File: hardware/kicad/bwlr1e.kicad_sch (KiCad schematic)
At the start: 66 parts, among them Q1 AO3407, Q2 DMG1012UW, SW3 RESET, SW4 BOOT, U1 BME680, U2 RAK3172, U3 AEM10941-QFN, U4 XC6215

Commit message: revision 2
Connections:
- net GND: now also SC1.2 (-), SC3.2 (-)
- net SOLAR+: now also SC2.1 (+), SC4.1 (+)
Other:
- note removed: "TODO: Change to Parallel"
- moved on the sheet: BT1, C1, C2, C4, C6, C7, C8, JP3, JP4, L2, L3, Q1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

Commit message: revision 3
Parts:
- added TP12: PRIMIN, TestPoint:TestPoint_Pad_D2.0mm, symbol Connector:TestPoint
- added TP13: GND, TestPoint:TestPoint_Pad_D2.0mm, symbol Connector:TestPoint
- TP1: value 3V3 -> PRIMIN
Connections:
- net GND: now also TP13.1
- net EXT_3V3 renamed PRIMIN
- net PRIMIN: now also TP12.1
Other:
- note added: "Options: 1. R10 = 1M, R11 = 100K, R14 = 400K, R15 = 1M, JP5 = PRIMIN 2. R10, R11, R14, and R15 = 0, R16, JP5 = Open 3. R10 = 1M, R11 = 100K, R14 = 400K, R15 = 1M, JP5 = BUCK"
- note added: "Primary Battery"
- note removed: "Experimental Options: 1. R10 = 1M, R11 = 100K, R14 = 400K, R15 = 1M, JP5 = EXT_3V3 2. R10, R11, R14, and R15 = 0, R16, JP5 = Open 3. R10 = 1M, R11 = 100K, R14 = 400K, R15 = 1M, JP5 = BUCK"
- note removed: "External Charging"
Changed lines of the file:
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@@
   (title_block
     (title "Teapot BWLR1E")
-    (date "2022-08-03")
-    (rev "2")
+    (date "2022-08-21")
+    (rev "3")
     (company "Teapot Laboratories")
   )
@@
     (stroke (width 0) (type default) (color 0 0 0 0))
   )
+  (wire (pts (xy 396.875 69.85) (xy 408.305 69.85))
+    (stroke (width 0) (type default) (color 0 0 0 0))
+  )
   (wire (pts (xy 138.43 121.92) (xy 138.43 127))
     (stroke (width 0) (type default) (color 0 0 0 0))
@@
     (stroke (width 0) (type default) (color 0 0 0 0))
   )
+  (wire (pts (xy 396.875 74.295) (xy 404.495 74.295))
+    (stroke (width 0) (type default) (color 0 0 0 0))
+  )
   (wire (pts (xy 86.36 165.1) (xy 86.36 166.37))
     (stroke (width 0) (type default) (color 0 0 0 0))
@@
     (effects (font (size 1.27 1.27)) (justify left bottom))
   )
-  (text "External Charging" (at 394.97 86.36 0)
+  (text "Primary Battery" (at 396.875 86.36 0)
     (effects (font (size 1.27 1.27)) (justify left bottom))
   )
@@
     (effects (font (size 1.27 1.27)) (justify left bottom))
   )
-  (text "Experimental Options:\n1. R10 = 1M, R11 = 100K, R14 = 400K, R15 = 1M, JP5 = EXT_3V3\n2. R10, R11, R14, and R15 = 0, R16, JP5 = Open\n3. R10 = 1M, R11 = 100K, R14 = 400K, R15 = 1M, JP5 = BUCK"
+  (text "Options:\n1. R10 = 1M, R11 = 100K, R14 = 400K, R15 = 1M, JP5 = PRIMIN\n2. R10, R11, R14, and R15 = 0, R16, JP5 = Open\n3. R10 = 1M, R11 = 100K, R14 = 400K, R15 = 1M, JP5 = BUCK"
     (at 343.535 19.685 0)
     (effects (font (size 1 1)) (justify left bottom))
@@
     (effects (font (size 1.27 1.27)) (justify left bottom))
   )
-  (label "EXT_3V3" (at 297.18 103.505 180)
+  (label "PRIMIN" (at 297.18 103.505 180)
     (effects (font (size 1.27 1.27)) (justify right bottom))
   )
@@
     (effects (font (size 1.27 1.27)) (justify right bottom))
   )
-  (label "EXT_3V3" (at 382.905 59.055 180)
+  (label "PRIMIN" (at 382.905 59.055 180)
     (effects (font (size 1.27 1.27)) (justify right bottom))
   )
@@
     (effects (font (size 1.27 1.27)) (justify left bottom))
   )
-  (label "EXT_3V3" (at 407.035 46.355 180)
+  (label "PRIMIN" (at 407.035 46.355 180)
     (effects (font (size 1.27 1.27)) (justify right bottom))
   )
@@
     (effects (font (size 1.27 1.27)) (justify right bottom))
   )
+  (label "PRIMIN" (at 408.305 69.85 180)
+    (effects (font (size 1.27 1.27)) (justify right bottom))
+  )
   (label "USER1" (at 223.52 166.37 180)
     (effects (font (size 1.27 1.27)) (justify right bottom))
@@
     (pin "2")
   )
+  (symbol (lib_id "power:GND") (at 404.495 74.295 0) (unit 1)
+    (in_bom yes) (on_board yes) (fields_autoplaced)
+    (property "Reference" "#PWR0135" (id 0) (at 404.495 80.645 0)
+      (effects (font (size 1.27 1.27)) hide)
+    )
+    (property "Value" "GND" (id 1) (at 404.495 79.375 0))
+    (property "Footprint" "" (id 2) (at 404.495 74.295 0)
+      (effects (font (size 1.27 1.27)) hide)
+    )
+    (property "Datasheet" "" (id 3) (at 404.495 74.295 0)
+      (effects (font (size 1.27 1.27)) hide)
+    )
+    (pin "1")
+  )
   (symbol (lib_id "Device:LED") (at 281.305 170.815 180) (unit 1)
     (in_bom yes) (on_board yes)
@@
     (in_bom yes) (on_board yes)
     (property "Reference" "TP1" (id 0) (at 271.78 103.505 90))
-    (property "Value" "3V3" (id 1) (at 278.13 103.505 90))
+    (property "Value" "PRIMIN" (id 1) (at 278.13 103.505 90))
     (property "Footprint" "TestPoint:TestPoint_Pad_1.5x1.5mm" (id 2) (at 285.75 98.425 0)
       (effects (font (size 1.27 1.27)) hide)
@@
     (pin "1")
   )
+  (symbol (lib_id "Connector:TestPoint") (at 396.875 74.295 90) (unit 1)
+    (in_bom yes) (on_board yes)
+    (property "Reference" "TP13" (id 0) (at 382.905 74.295 90))
+    (property "Value" "GND" (id 1) (at 389.255 74.295 90))
+    (property "Footprint" "TestPoint:TestPoint_Pad_D2.0mm" (id 2) (at 396.875 69.215 0)
+      (effects (font (size 1.27 1.27)) hide)
+    )
+    (property "Datasheet" "~" (id 3) (at 396.875 69.215 0)
+      (effects (font (size 1.27 1.27)) hide)
+    )
+    (pin "1")
+  )
   (symbol (lib_id "power:GND") (at 194.945 121.92 0) (unit 1)
     (in_bom yes) (on_board yes)
@@
     (pin "3")
   )
+  (symbol (lib_id "Connector:TestPoint") (at 396.875 69.85 90) (unit 1)
+    (in_bom yes) (on_board yes)
+    (property "Reference" "TP12" (id 0) (at 382.905 69.85 90))
+    (property "Value" "PRIMIN" (id 1) (at 389.255 69.85 90))
+    (property "Footprint" "TestPoint:TestPoint_Pad_D2.0mm" (id 2) (at 396.875 64.77 0)
+      (effects (font (size 1.27 1.27)) hide)
+    )
+    (property "Datasheet" "~" (id 3) (at 396.875 64.77 0)
+      (effects (font (size 1.27 1.27)) hide)
+    )
+    (pin "1")
+  )
   (symbol (lib_id "power:GND") (at 48.26 134.62 0) (unit 1)
     (in_bom yes) (on_board yes) (fields_autoplaced)
@@
       (reference "#PWR0134") (unit 1) (value "+3V3") (footprint "")
     )
+    (path "/1e90f9d8-c727-4558-8e6d-fc3c11796233"
+      (reference "#PWR0135") (unit 1) (value "GND") (footprint "")
+    )
     (path "/c9f4c90b-d12e-49a7-861d-d88f5120271b"
       (reference "BT1") (unit 1) (value "3.7v LiPo") (footprint "Connector_JST:JST_PH_S2B-PH-K_1x02_P2.00mm_Horizontal")
@@
     )
     (path "/2a1338b5-8d40-458a-9d24-bac76b51b578"
-      (reference "TP1") (unit 1) (value "3V3") (footprint "TestPoint:TestPoint_Pad_1.5x1.5mm")
+      (reference "TP1") (unit 1) (value "PRIMIN") (footprint "TestPoint:TestPoint_Pad_1.5x1.5mm")
     )
     (path "/b524f92a-354c-4e70-b2ab-52ea6b8a451a"
@@
       (reference "TP11") (unit 1) (value "SOLAR-") (footprint "TestPoint:TestPoint_Pad_D1.5mm")
     )
+    (path "/81b383ec-6014-4264-9dd9-3b100f125f97"
+      (reference "TP12") (unit 1) (value "PRIMIN") (footprint "TestPoint:TestPoint_Pad_D2.0mm")
+    )
+    (path "/5e32705b-900d-4567-9e7f-6cf99fe286b8"
+      (reference "TP13") (unit 1) (value "GND") (footprint "TestPoint:TestPoint_Pad_D2.0mm")
+    )
     (path "/33f66e46-4d60-4c90-84ca-37ca92e2ffdc"

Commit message: move battery measurement to PB3
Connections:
- net BATT_MEAS: now also U2.32 (PB3/ADC1); no longer U2.3 (PA15/ADC5)
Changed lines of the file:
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@@
   (no_connect (at 67.31 154.94))
   (no_connect (at 67.31 134.62))
-  (no_connect (at 67.31 132.08))
+  (no_connect (at 67.31 142.24))
   (no_connect (at 118.11 137.16))
   (no_connect (at 118.11 139.7))
@@
     (stroke (width 0) (type default) (color 0 0 0 0))
   )
-  (wire (pts (xy 55.88 142.24) (xy 67.31 142.24))
+  (wire (pts (xy 55.88 132.08) (xy 67.31 132.08))
     (stroke (width 0) (type default) (color 0 0 0 0))
   )
@@
     (effects (font (size 1.27 1.27)) (justify right bottom))
   )
-  (label "BATT_MEAS" (at 55.88 142.24 0)
-    (effects (font (size 1.27 1.27)) (justify left bottom))
-  )
+  (label "BATT_MEAS" (at 55.88 132.08 0)
+    (effects (font (size 1.27 1.27)) (justify left bottom))
+  )

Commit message: change jst type to smt
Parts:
- BT1: value 3.7v LiPo -> (none); footprint Connector_JST:JST_PH_S2B-PH-K_1x02_P2.00mm_Horizontal -> (none)
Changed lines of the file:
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@@
   (title_block
     (title "Teapot BWLR1E")
-    (date "2022-08-21")
-    (rev "3")
+    (date "2022-10-22")
+    (rev "4")
     (company "Teapot Laboratories")
   )
@@
       (effects (font (size 1.27 1.27)) (justify left))
     )
-    (property "Value" "3.7v LiPo" (id 1) (at 36.195 70.9929 0)
+    (property "Value" "" (id 1) (at 36.195 70.9929 0)
       (effects (font (size 1.27 1.27)) (justify left))
     )
-    (property "Footprint" "Connector_JST:JST_PH_S2B-PH-K_1x02_P2.00mm_Horizontal" (id 2) (at 32.385 70.231 90)
+    (property "Footprint" "" (id 2) (at 32.385 70.231 90)
       (effects (font (size 1.27 1.27)) hide)
     )
@@
     )
     (path "/c9f4c90b-d12e-49a7-861d-d88f5120271b"
-      (reference "BT1") (unit 1) (value "3.7v LiPo") (footprint "Connector_JST:JST_PH_S2B-PH-K_1x02_P2.00mm_Horizontal")
+      (reference "BT1") (unit 1) (value "3.7v LiPo") (footprint "Connector_JST:JST_PH_S2B-PH-SM4-TB_1x02-1MP_P2.00mm_Horizontal")
     )
     (path "/0befad4f-2e6c-4a2e-8b15-04b1327638c6"

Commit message: improve layout and silkscreen info
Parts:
- removed JP5: FB_PRIM_EN, Jumper:SolderJumper-3_P1.3mm_Open_RoundedPad1.0x1.5mm_NumberLabels, symbol Jumper:SolderJumper_3_Open
- removed R10, R15: 1M, Resistor_SMD:R_0603_1608Metric_Pad0.98x0.95mm_HandSolder, symbol Device:R_Small
- removed R11: 100K, Resistor_SMD:R_0603_1608Metric_Pad0.98x0.95mm_HandSolder, symbol Device:R_Small
- removed R14: 400K, Resistor_SMD:R_0603_1608Metric_Pad0.98x0.95mm_HandSolder, symbol Device:R_Small
- removed R16: 0, Resistor_SMD:R_0603_1608Metric_Pad0.98x0.95mm_HandSolder, symbol Device:R_Small
- removed TP12: PRIMIN, TestPoint:TestPoint_Pad_D2.0mm, symbol Connector:TestPoint
- removed TP13: GND, TestPoint:TestPoint_Pad_D2.0mm, symbol Connector:TestPoint
- added TP14: BOOT, TestPoint:TestPoint_Pad_D1.0mm, symbol Connector:TestPoint
- BT1: value (none) -> 3.7v LiPo; footprint (none) -> Connector_JST:JST_PH_S2B-PH-SM4-TB_1x02-1MP_P2.00mm_Horizontal
- C1, C11, C12, C3, C5: value 100nF -> 100n
- C13, C14, C17, C8: value 10uF -> 10u
- C6: value 150uF -> 150u
- C7: value 22uF -> 22u
- JP1: footprint Jumper:SolderJumper-3_P1.3mm_Bridged12_RoundedPad1.0x1.5mm_NumberLabels -> Jumper:SolderJumper-3_P1.3mm_Bridged12_RoundedPad1.0x1.5mm
- JP2: footprint Jumper:SolderJumper-3_P1.3mm_Bridged12_RoundedPad1.0x1.5mm_NumberLabels -> Jumper:SolderJumper-3_P1.3mm_Open_RoundedPad1.0x1.5mm; symbol Jumper:SolderJumper_3_Bridged12 -> Jumper:SolderJumper_3_Open
- L3: value 10uH -> 10u
- TP1: value PRIMIN -> LIPO+; footprint TestPoint:TestPoint_Pad_1.5x1.5mm -> TestPoint:TestPoint_Pad_D1.0mm
- TP2, TP3, TP4, TP5, TP6, TP7: footprint TestPoint:TestPoint_Pad_1.5x1.5mm -> TestPoint:TestPoint_Pad_D1.0mm
- TP8, TP9: footprint TestPoint:TestPoint_Pad_D1.5mm -> TestPoint:TestPoint_Pad_D1.0mm
- U1: value BME680 -> BME688
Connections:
- net FB_PRIM_D is gone; now on net GND: U3.9 (FB_PRIM_D)
- net FB_PRIM_U is gone; now on net GND: U3.10 (FB_PRIM_U)
- net PRIM is gone; now on net GND: U3.17 (PRIM)
- net PRIMIN is gone; now on net LIPO+: TP1.1
- net +3V3: now also SW4.2
- net BATT+: now also TP9.1
- net GND: no longer SW4.2
- net LED1: now also U2.3 (PA15/ADC5); no longer U2.29 (PA0)
- net LED2: now also U2.4 (UART1_TX/PB6); no longer U2.6 (PA1)
- net USER0: now also U2.25 (PA10/ADC4); no longer U2.20 (PA9)
- net USER1: now also U2.26 (PB2/ADC3); no longer U2.19 (PA8)
- net BOOT: now reaches SW4.1, U2.21 (BOOT0)
- net BOOT: now also TP14.1
- net ANT: now reaches C16.2, E1.1, L1.2
- net LIPO+: now reaches BT1.1 (+), C2.1, C4.1, Q1.3 (D)
- net LIPO+: no longer TP9.1
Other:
- note added: "BME688 Environmental Sensor"
- note added: "Battery Input and Polar Protection"
- note added: "Coplanar Waveguide With Ground Characteristic"
- note added: "Effective Dielectric Constant: 2.8 Characteristic Impedance: 50.27ohm"
- note added: "I2C Address: 0x77"
- note added: "Relative Dielectric Constant: 4.5 Track Width : 1mm Gap Width : 0.15mm Dielectric Thickness : 1.6mm"
- note added: "Trace characteristics"
- note added: "User Configuration"
- note removed: "3.7v LiPo Battery Input and Polar Protection"
- note removed: "BME680 Environmental Sensor over I2C"
- note removed: "Options: 1. R10 = 1M, R11 = 100K, R14 = 400K, R15 = 1M, JP5 = PRIMIN 2. R10, R11, R14, and R15 = 0, R16, JP5 = Open 3. R10 = 1M, R11 = 100K, R14 = 400K, R15 = 1M, JP5 = BUCK"
- note removed: "Primary Battery"
- note removed: "User Input"
- moved on the sheet: C1, C13, C14, C6, C7, C8, L2, L3, R1, R4, TP1, TP2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

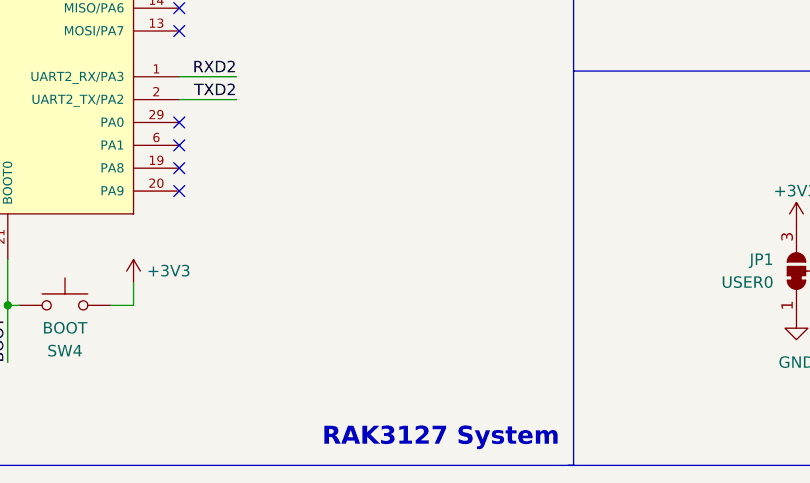
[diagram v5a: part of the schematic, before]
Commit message: added qwiic connector
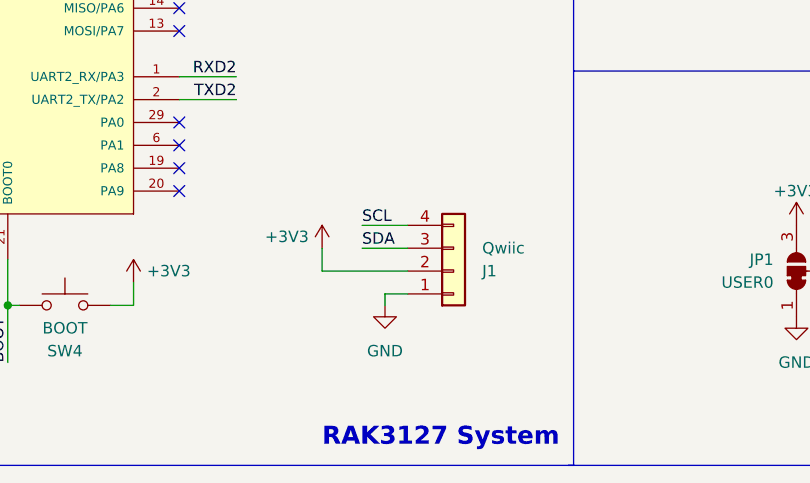
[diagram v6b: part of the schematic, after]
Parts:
- added J1: Qwiic, Connector_JST:JST_SH_SM04B-SRSS-TB_1x04-1MP_P1.00mm_Horizontal, symbol Connector_Generic:Conn_01x04
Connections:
- net +3V3: now also J1.2 (Pin_2)
- net GND: now also J1.1 (Pin_1)
- net SCL: now also J1.4 (Pin_4)
- net SDA: now also J1.3 (Pin_3)
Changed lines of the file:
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@@
+    (stroke (width 0) (type default))
+  )
+  (wire (pts (xy 133.985 166.37) (xy 143.51 166.37))
     (stroke (width 0) (type default))
   )
@@
     (stroke (width 0) (type default))
   )
+  (wire (pts (xy 138.43 161.29) (xy 143.51 161.29))
+    (stroke (width 0) (type default))
+  )
+  (wire (pts (xy 140.97 168.91) (xy 140.97 170.18))
+    (stroke (width 0) (type default))
+  )
   (wire (pts (xy 260.35 22.86) (xy 278.13 22.86))
     (stroke (width 0) (type default))
@@
     (stroke (width 0) (type default))
   )
+  (wire (pts (xy 133.985 163.83) (xy 133.985 166.37))
+    (stroke (width 0) (type default))
+  )
   (polyline (pts (xy 161.925 12.065) (xy 161.925 87.63))
     (stroke (width 0) (type default))
@@
     (stroke (width 0) (type default))
   )
+  (wire (pts (xy 138.43 163.83) (xy 143.51 163.83))
+    (stroke (width 0) (type default))
+  )
   (wire (pts (xy 219.71 45.72) (xy 196.85 45.72))
     (stroke (width 0) (type default))
@@
   )
   (polyline (pts (xy 161.925 144.145) (xy 238.76 144.145))
+    (stroke (width 0) (type default))
+  )
+  (wire (pts (xy 143.51 168.91) (xy 140.97 168.91))
     (stroke (width 0) (type default))
   )
@@
     (effects (font (size 1.27 1.27)) (justify left bottom))
   )
+  (label "SCL" (at 138.43 161.29 0) (fields_autoplaced)
+    (effects (font (size 1.27 1.27)) (justify left bottom))
+  )
   (label "LDO_EN" (at 269.875 60.96 180) (fields_autoplaced)
     (effects (font (size 1.27 1.27)) (justify right bottom))
@@
   )
   (label "BUCK" (at 214.63 53.34 0) (fields_autoplaced)
+    (effects (font (size 1.27 1.27)) (justify left bottom))
+  )
+  (label "SDA" (at 138.43 163.83 0) (fields_autoplaced)
     (effects (font (size 1.27 1.27)) (justify left bottom))
   )
@@
     )
   )
+  (symbol (lib_id "Connector_Generic:Conn_01x04") (at 148.59 166.37 0) (mirror x) (unit 1)
+    (in_bom yes) (on_board yes) (dnp no)
+    (property "Reference" "J1" (at 151.765 166.37 0)
+      (effects (font (size 1.27 1.27)) (justify left))
+    )
+    (property "Value" "Qwiic" (at 151.765 163.83 0)
+      (effects (font (size 1.27 1.27)) (justify left))
+    )
+    (property "Footprint" "Connector_JST:JST_SH_SM04B-SRSS-TB_1x04-1MP_P1.00mm_Horizontal" (at 148.59 166.37 0)
+      (effects (font (size 1.27 1.27)) hide)
+    )
+    (property "Datasheet" "~" (at 148.59 166.37 0)
+      (effects (font (size 1.27 1.27)) hide)
+    )
+    (pin "1")
+    (pin "2")
+    (pin "3")
+    (pin "4")
+    (instances
+      (project "bwlr1e"
+        (path "/630c8da6-5464-4eef-824d-89618087f4b4"
+          (reference "J1") (unit 1)
+        )
+      )
+    )
+  )
   (symbol (lib_id "power:GND") (at 264.16 77.47 0) (unit 1)
     (in_bom yes) (on_board yes) (dnp no)
@@
     )
   )
+  (symbol (lib_id "power:+3V3") (at 133.985 163.83 0) (mirror y) (unit 1)
+    (in_bom yes) (on_board yes) (dnp no)
+    (property "Reference" "#PWR07" (at 133.985 167.64 0)
+      (effects (font (size 1.27 1.27)) hide)
+    )
+    (property "Value" "+3V3" (at 127.635 162.56 0)
+      (effects (font (size 1.27 1.27)) (justify right))
+    )
+    (property "Footprint" "" (at 133.985 163.83 0)
+      (effects (font (size 1.27 1.27)) hide)
+    )
+    (property "Datasheet" "" (at 133.985 163.83 0)
+      (effects (font (size 1.27 1.27)) hide)
+    )
+    (pin "1")
+    (instances
+      (project "bwlr1e"
+        (path "/630c8da6-5464-4eef-824d-89618087f4b4"
+          (reference "#PWR07") (unit 1)
+        )
+      )
+    )
+  )
   (symbol (lib_id "power:GND") (at 196.85 60.96 0) (unit 1)
     (in_bom yes) (on_board yes) (dnp no)
@@
         )
       )
+    )
+  )
+  (symbol (lib_id "power:GND") (at 140.97 170.18 0) (unit 1)
+    (in_bom yes) (on_board yes) (dnp no) (fields_autoplaced)
+    (property "Reference" "#PWR05" (at 140.97 176.53 0)
+      (effects (font (size 1.27 1.27)) hide)
+    )
+    (property "Value" "GND" (at 140.97 175.26 0)
+      (effects (font (size 1.27 1.27)))
+    )
+    (property "Footprint" "" (at 140.97 170.18 0)
+      (effects (font (size 1.27 1.27)) hide)
+    )
+    (property "Datasheet" "" (at 140.97 170.18 0)
+      (effects (font (size 1.27 1.27)) hide)
+    )
+    (pin "1")
+    (instances
+      (project "bwlr1e"
+        (path "/630c8da6-5464-4eef-824d-89618087f4b4"
+          (reference "#PWR05") (unit 1)
+        )
+      )

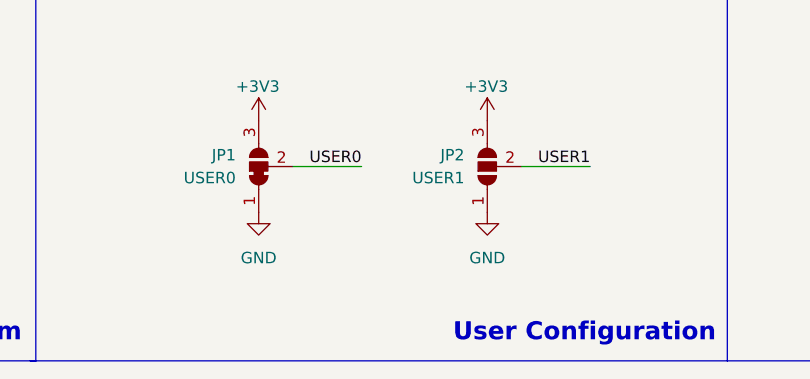
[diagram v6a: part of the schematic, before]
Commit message: improve silkscreen graphic and wiring
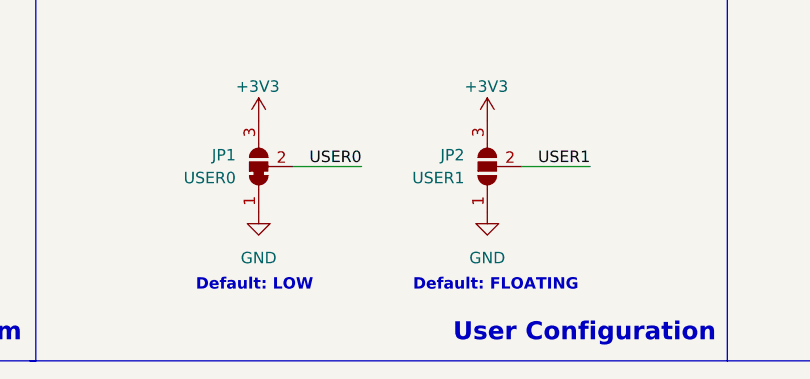
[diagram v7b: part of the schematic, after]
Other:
- note added: "Default: FLOATING"
- note added: "Default: LOW"
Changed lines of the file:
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@@
     (effects (font (size 2 2) (thickness 0.4) bold) (justify left bottom))
+  )
+  (text "Default: FLOATING" (at 203.835 180.34 0)
+    (effects (font (size 1.27 1.27) bold) (justify left bottom))
+  )
+  (text "Default: LOW" (at 179.705 180.34 0)
+    (effects (font (size 1.27 1.27) bold) (justify left bottom))
   )
   (text "Battery Measurement" (at 128.27 86.36 0)
